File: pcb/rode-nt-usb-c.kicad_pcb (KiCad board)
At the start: 2 copper layers, 36 x 15 mm, 7 parts, among them J2 Conn_01x05_Pin, J3 USB_C_Receptacle_USB2.0_16P

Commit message: rearrange files
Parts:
- renumbered J3 to J1

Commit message: Add production files
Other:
- board text added: "WayWayWay"

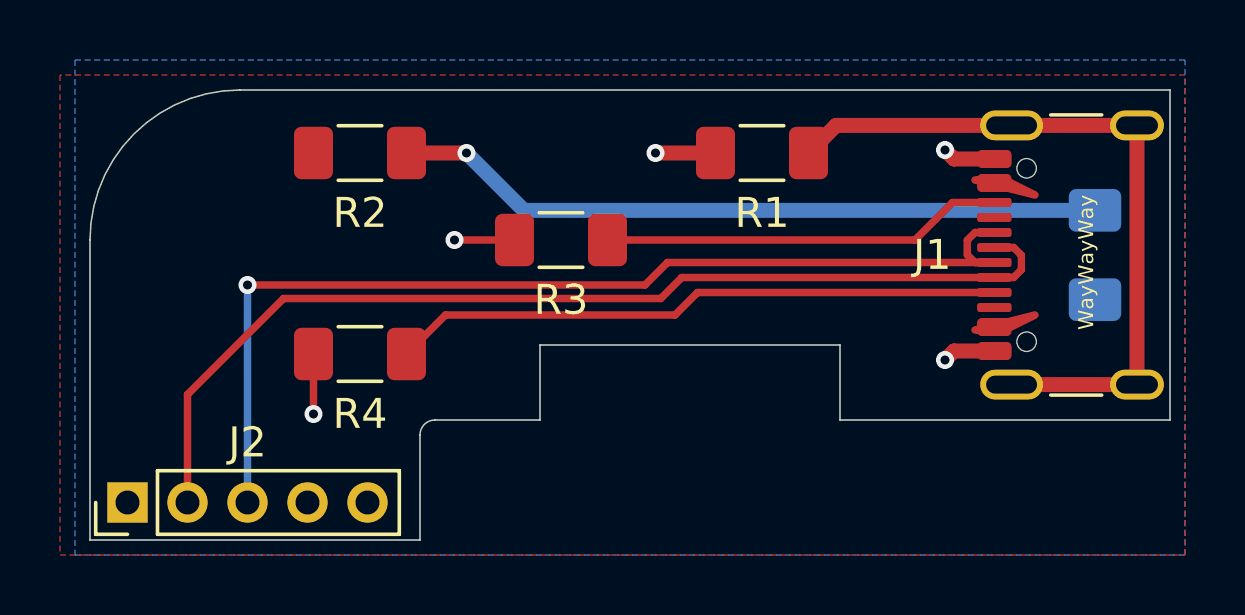
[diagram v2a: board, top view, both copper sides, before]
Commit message: Remove R1, update overall design
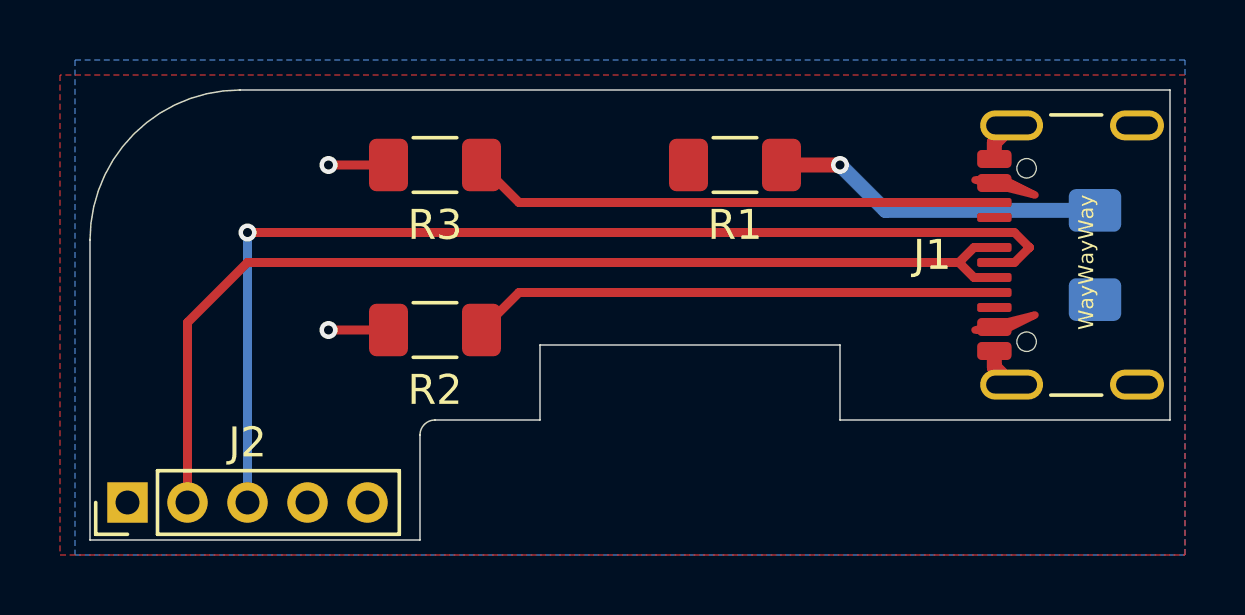
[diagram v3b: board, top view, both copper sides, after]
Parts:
- removed the R1 at (98.4, 55.6)
- moved R1 12.5 mm to (97.5, 56.0)
- moved R3 4.89 mm to (87.5, 56.0)
- moved R2 2.62 mm to (87.5, 61.5)
- renumbered R2 to R1, R4 to R2
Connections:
- J1 pad S1: Net-(J1-SHIELD) -> GND
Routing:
- net Net-(J1-SHIELD): track 24.2 -> 0.00 mm
- net Net-(D1-A): track 23.7 -> 11.1 mm
- net Net-(J1-CC2): track 13.4 -> 17.6 mm
- net Net-(J1-CC1): track 20.4 -> 17.6 mm
- net GND: track 9.54 -> 6.72 mm, vias 5 -> 2
- net D+: track 35.0 -> 36.7 mm
- net D-: track 34.6 -> 35.3 mm

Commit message: Change design, multiple adjustments
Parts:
- renumbered R3 to R2, R2 to R3
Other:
- board text added: "github.com/CityRunner/rode-nt-usb-c"
- board text removed: "https://github.com/CityRunner/rode-nt-usb-c"
